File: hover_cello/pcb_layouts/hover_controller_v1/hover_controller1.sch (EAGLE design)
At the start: 14 parts, among them IC2 L298, IC3 7805TV

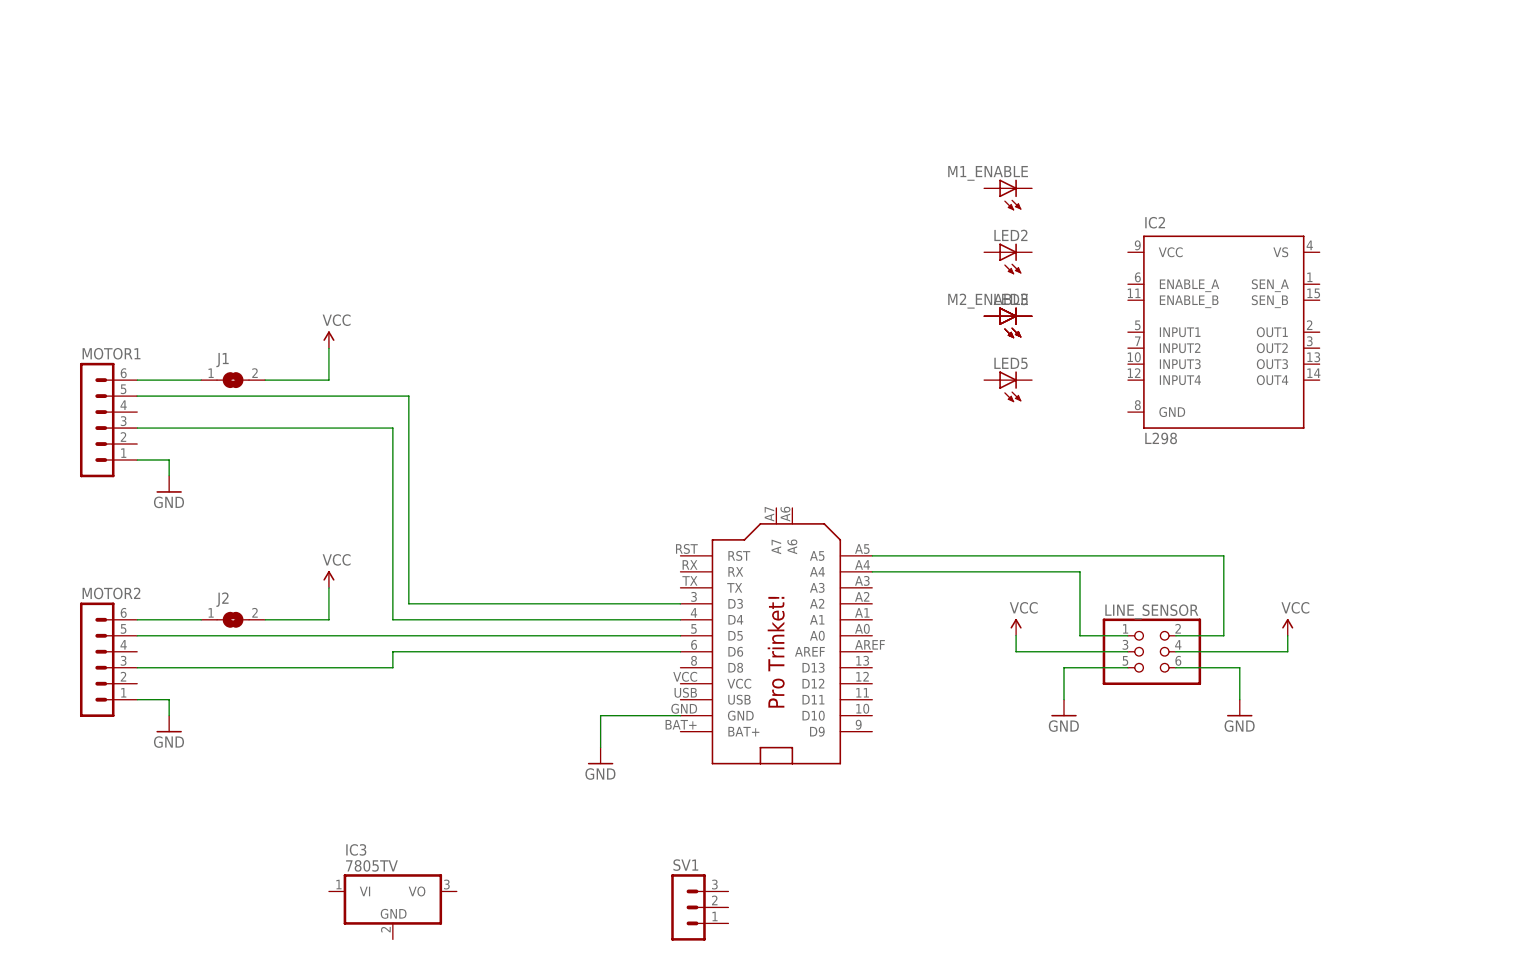
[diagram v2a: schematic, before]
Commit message: wrote basic thermal data visualizer in processing for D6T
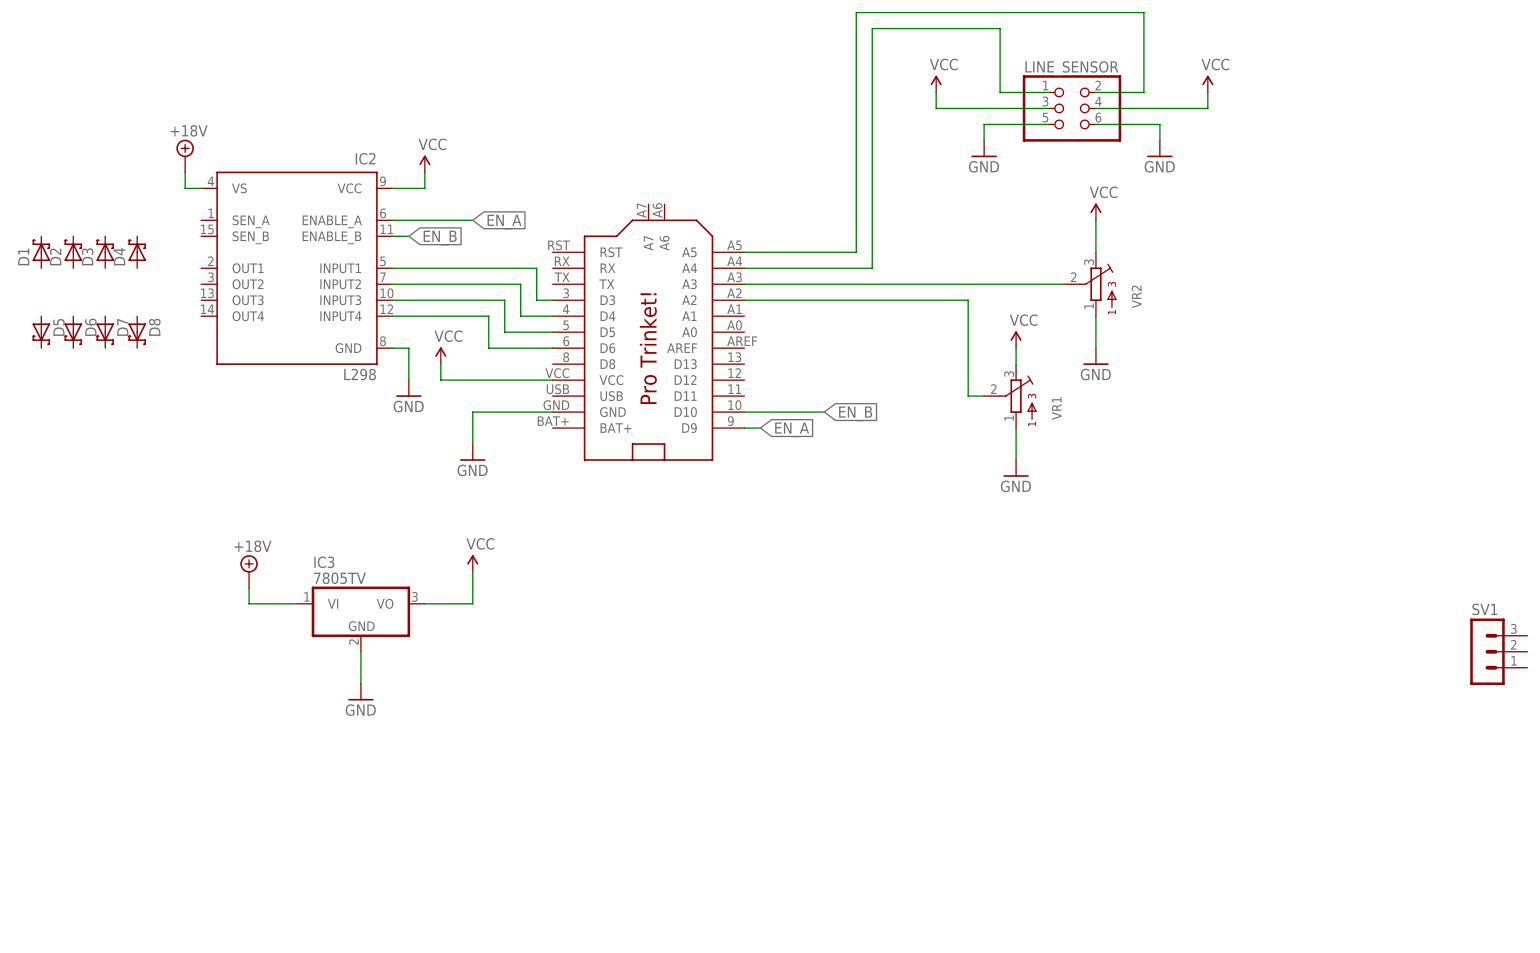
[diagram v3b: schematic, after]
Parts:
- removed J1, J2: (no value), jumper:SJW
- removed LED2, LED3, LED5, M1_ENABLE, M2_ENABLE: (no value), led:LED3MM
- removed MOTOR1, MOTOR2: HEADER-06X1-MALE, GeekAmmo:HEADER-06X1-MALE
- added D1, D2, D3, D4, D5, D6, D7, D8: (no value), diode:SCHOTTKY-DIODEDO35-7
- added VR1, VR2: (no value), MusicThingModular:BOURNS_3362P_TRIMMERP
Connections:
- removed net M1_DIRECTION: MOTOR1.3, U$1.D4
- removed net M1_ENABLE: MOTOR1.5, U$1.D3
- removed net M2_DIRECTION: MOTOR2.3, U$1.D6
- removed net M2_ENABLE: MOTOR2.5, U$1.D5
- new net +18V: IC2.VS, IC3.VI
- new net EN_A: IC2.ENABLE_A, U$1.D9
- new net EN_B: IC2.ENABLE_B, U$1.D10
- new net N$5: U$1.A3, VR2.2
- new net N$6: U$1.A2, VR1.2
- net GND: now also IC2.GND, IC3.GND, VR1.1, VR2.1; no longer MOTOR1.1, MOTOR2.1
- net N$1: now also IC2.INPUT1, U$1.D3; no longer J1.1, MOTOR1.6
- net N$2: now also IC2.INPUT2, U$1.D4; no longer J2.1, MOTOR2.6
- net N$3: now also IC2.INPUT3, U$1.D5; no longer LED3.C, M2_ENABLE.C
- net N$4: now also IC2.INPUT4, U$1.D6; no longer LED3.A, M2_ENABLE.A
- net VCC: now also IC2.VCC, IC3.VO, U$1.VCC, VR1.3, VR2.3; no longer J1.2, J2.2
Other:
- moved on the sheet: IC2, IC3, LINE_SENSOR, SV1
